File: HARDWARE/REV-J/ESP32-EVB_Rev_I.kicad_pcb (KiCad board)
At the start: 2 copper layers, 75.2 x 99.3 mm, 166 parts, among them CON1 TB3 DG306-5.0-3P, CON2 TB3 DG306-5.0-3P, Q1 BC817-40(SOT23), Q2 BC817-40(SOT23), Q3 Q12MHz/20pF/30ppm/2P/HC-49SM(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, Q4 BC817-40(SOT23), Q5 BC817-40(SOT23), Q6 BC817, Q7 BC817-40(SOT23), U1 BL4054B-42TPRN(SOT23-5), U10 BAT54C(SOT23-3), U2 SY8089AAAC(SOT23-5), U3 ESP-WROOM-32, U4 LAN8710A-EZC(QFN32), U5 CH340T(SSOP20W), U6 MCP2562-E/SN(SOIC-8_150mil), U7 RPM7236-H8, U8 NCP303LSN27T1G(SOT-23-5), U9 BAT54C(SOT23-3)

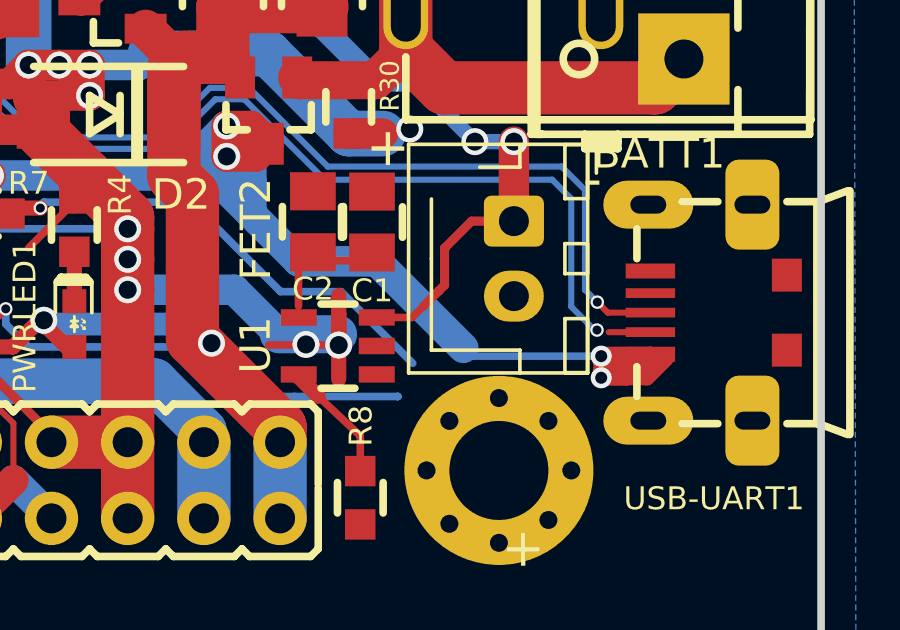
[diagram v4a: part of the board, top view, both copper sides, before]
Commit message: re-Route batrai charging
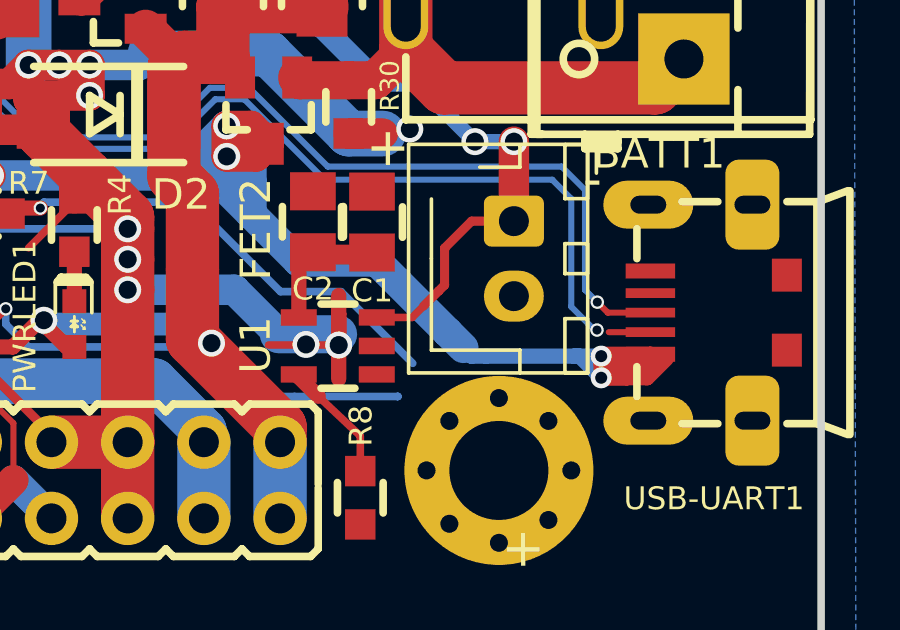
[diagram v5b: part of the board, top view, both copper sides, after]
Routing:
- net +5V: track 128.9 -> 133.3 mm
- net /+5V_USB: track 95.2 -> 97.5 mm
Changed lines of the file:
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@@
     (thickness 1.6)
     (drawings 137)
-    (tracks 3590)
+    (tracks 3600)
     (zones 0)
     (modules 166)
@@
   (segment (start 124.094 131.636) (end 123.825 131.905) (width 0.254) (layer F.Cu) (net 1))
   (segment (start 123.825 134.239) (end 123.825 131.905) (width 1.778) (layer F.Cu) (net 1))
+  (segment (start 127.37 131.806) (end 127.84 131.336) (width 0.508) (layer F.Cu) (net 1))
+  (segment (start 127.37 133.51) (end 127.37 131.806) (width 0.508) (layer F.Cu) (net 1))
+  (segment (start 129.8 131.336) (end 129.81 131.346) (width 0.508) (layer F.Cu) (net 1))
+  (segment (start 127.84 131.336) (end 129.8 131.336) (width 0.508) (layer F.Cu) (net 1))
   (segment (start 78.309 119.54) (end 80.424 119.54) (width 0.508) (layer F.Cu) (net 2) (status 40000))
   (segment (start 80.424 119.54) (end 80.899 120.015) (width 0.508) (layer F.Cu) (net 2) (status 40000))
@@
   (segment (start 137.45 135.521) (end 138.979 135.521) (width 0.508) (layer F.Cu) (net 82))
   (via (at 137.45 135.521) (size 0.7) (drill 0.4) (layers F.Cu B.Cu) (net 82))
-  (segment (start 137.45 135.521) (end 137.45 134.8) (width 0.508) (layer B.Cu) (net 82))
   (segment (start 74.168 130.429) (end 74.168 130.683) (width 1.016) (layer F.Cu) (net 83) (status 40000))
   (segment (start 74.168 130.683) (end 76.835 133.35) (width 1.016) (layer F.Cu) (net 83) (status 40000))
@@
   (segment (start 124.968 128.143) (end 124.968 129.618) (width 0.254) (layer B.Cu) (net 82))
   (segment (start 124.968 129.618) (end 126.99 131.64) (width 0.254) (layer B.Cu) (net 82))
-  (segment (start 133.13 134.8) (end 137.45 134.8) (width 0.254) (layer B.Cu) (net 82))
   (segment (start 126.99 131.64) (end 127.36 131.64) (width 0.254) (layer B.Cu) (net 82))
-  (segment (start 129.97 131.64) (end 132.855 134.525) (width 1.016) (layer B.Cu) (net 82))
   (segment (start 127.36 131.64) (end 129.97 131.64) (width 1.016) (layer B.Cu) (net 82))
-  (segment (start 132.855 134.525) (end 133.13 134.8) (width 0.254) (layer B.Cu) (net 82))
   (segment (start 125.79 130.07) (end 125.79 128.972) (width 1.016) (layer B.Cu) (net 82))
   (segment (start 124.968 129.248) (end 125.79 130.07) (width 1.016) (layer B.Cu) (net 82))
@@
   (segment (start 124.968 128.832) (end 124.968 129.248) (width 1.016) (layer B.Cu) (net 82))
   (segment (start 122.622 128.778) (end 121.793 128.778) (width 1.016) (layer B.Cu) (net 82))
+  (segment (start 132.855 134.525) (end 133.13 134.8) (width 0.508) (layer B.Cu) (net 82))
+  (segment (start 136.729 134.8) (end 136.55 134.8) (width 0.508) (layer B.Cu) (net 82))
+  (segment (start 137.45 135.521) (end 136.729 134.8) (width 0.508) (layer B.Cu) (net 82))
+  (segment (start 136.55 134.8) (end 137.45 134.8) (width 0.508) (layer B.Cu) (net 82))
+  (segment (start 137.45 135.521) (end 137.45 134.8) (width 0.508) (layer B.Cu) (net 82))
+  (segment (start 133.61 134.8) (end 133.13 134.8) (width 0.508) (layer B.Cu) (net 82))
+  (segment (start 132.33 134) (end 132.855 134.525) (width 1.016) (layer B.Cu) (net 82))
+  (segment (start 129.97 131.64) (end 132.33 134) (width 1.016) (layer B.Cu) (net 82))
+  (segment (start 133.61 134.8) (end 136.55 134.8) (width 0.508) (layer B.Cu) (net 82))
+  (segment (start 132.33 134) (end 133.13 134.8) (width 0.508) (layer B.Cu) (net 82))
   (segment (start 114.6048 118.6434) (end 114.0206 118.6434) (width 0.2032) (layer B.Cu) (net 99))
   (segment (start 136.91 132.580386) (end 136.91 129.26) (width 0.2032) (layer B.Cu) (net 99))

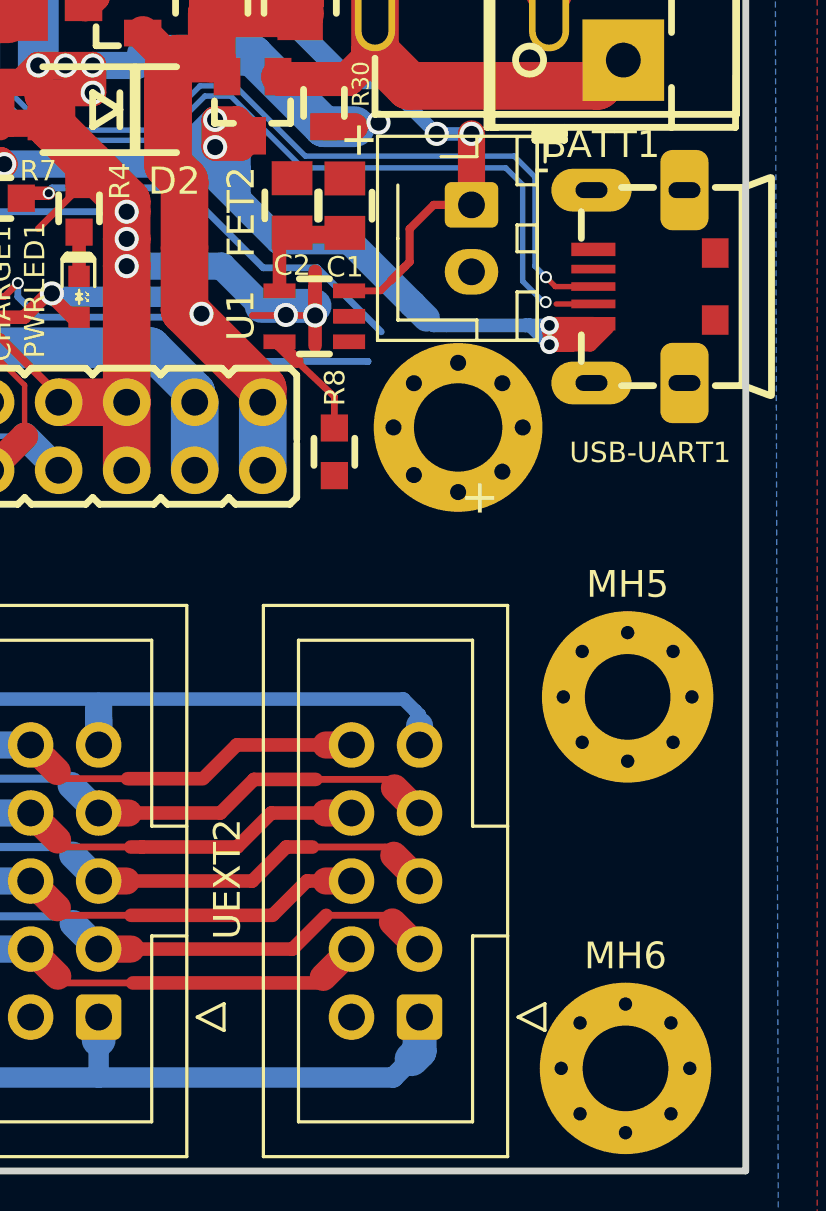
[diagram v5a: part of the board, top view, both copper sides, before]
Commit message: fix bat carging route
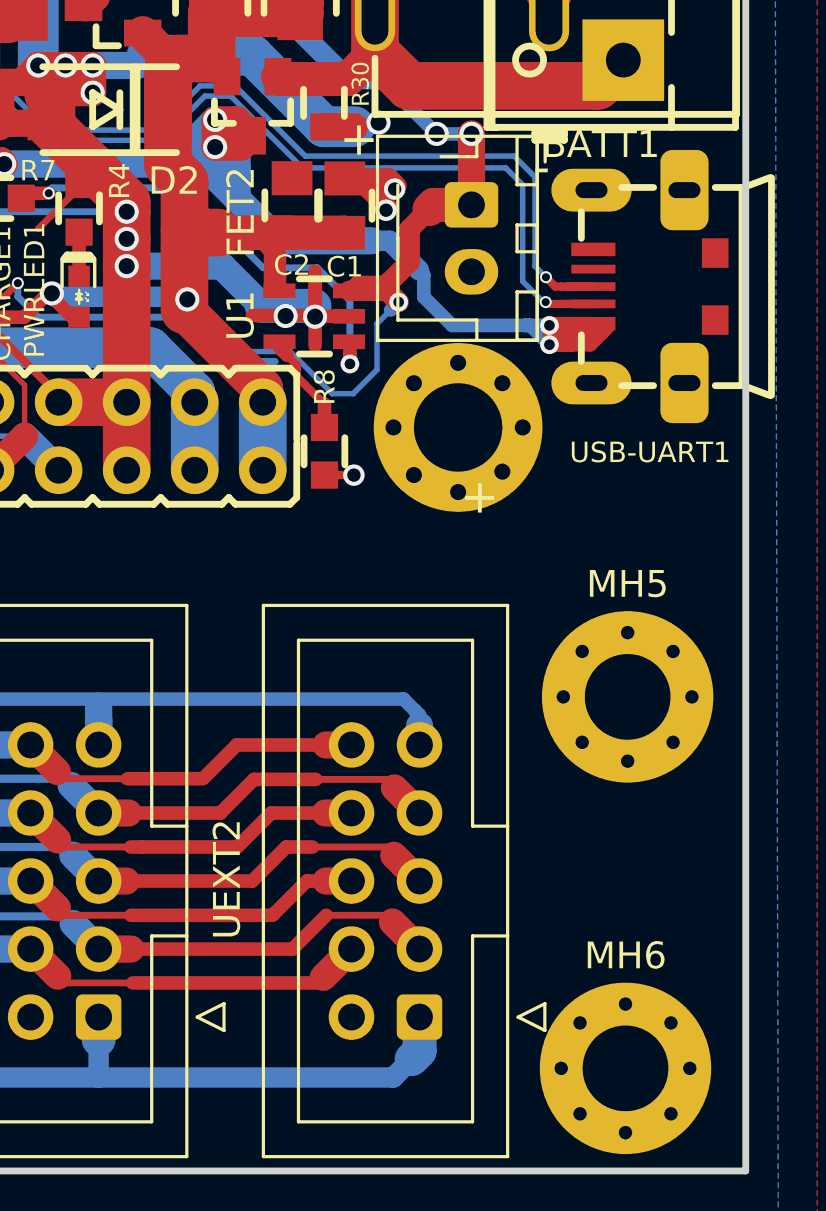
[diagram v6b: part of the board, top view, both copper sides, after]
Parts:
- moved R8 0.37 mm to (129.1, 139.5)
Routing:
- net +5V: track 133.3 -> 147.2 mm
- net Net-(BATT1-Pad1): track 61.5 -> 72.4 mm, vias 6 -> 7
- net GND: track 988.8 -> 995.6 mm, vias 131 -> 134
- net Net-(U5-Pad7): track 47.2 -> 52.0 mm
- net (no net): track 1.79 -> 0.00 mm
- net Net-(R7-Pad1): track 15.8 -> 17.4 mm, vias 1 -> 2
- net Net-(U5-Pad6): track 46.8 -> 48.2 mm
- net /+5V_USB: track 97.5 -> 96.9 mm

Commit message: Update ESP32-EVB_Rev_I.kicad_pcb, ESP32-EVB_Rev_I.kicad_pcb-bak, and _autosave-ESP32-EVB_Rev_I.kicad_pcb
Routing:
- net +3V3: track 243.8 -> 247.1 mm, vias 14 -> 15
- net Net-(BATT1-Pad1): track 72.4 -> 74.8 mm
- net Net-(U5-Pad7): track 52.0 -> 53.0 mm
- net Net-(U5-Pad6): track 48.2 -> 49.2 mm
- net GND: vias 134 -> 135

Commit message: Update ESP32-EVB_Rev_I.kicad_pcb, ESP32-EVB_Rev_I.kicad_pcb-bak, and _autosave-ESP32-EVB_Rev_I.kicad_pcb
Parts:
- moved MH3 0.72 mm to (73.3, 138.6)
